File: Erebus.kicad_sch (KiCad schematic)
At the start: 28 parts, among them SW1 SW_SPST, U1 AMS1117-3.3, U2 H5VU25U, U3 H5VU25U, U4 AT32F415CBT7, U5 STM32F303CBTx, Y1 8MHz

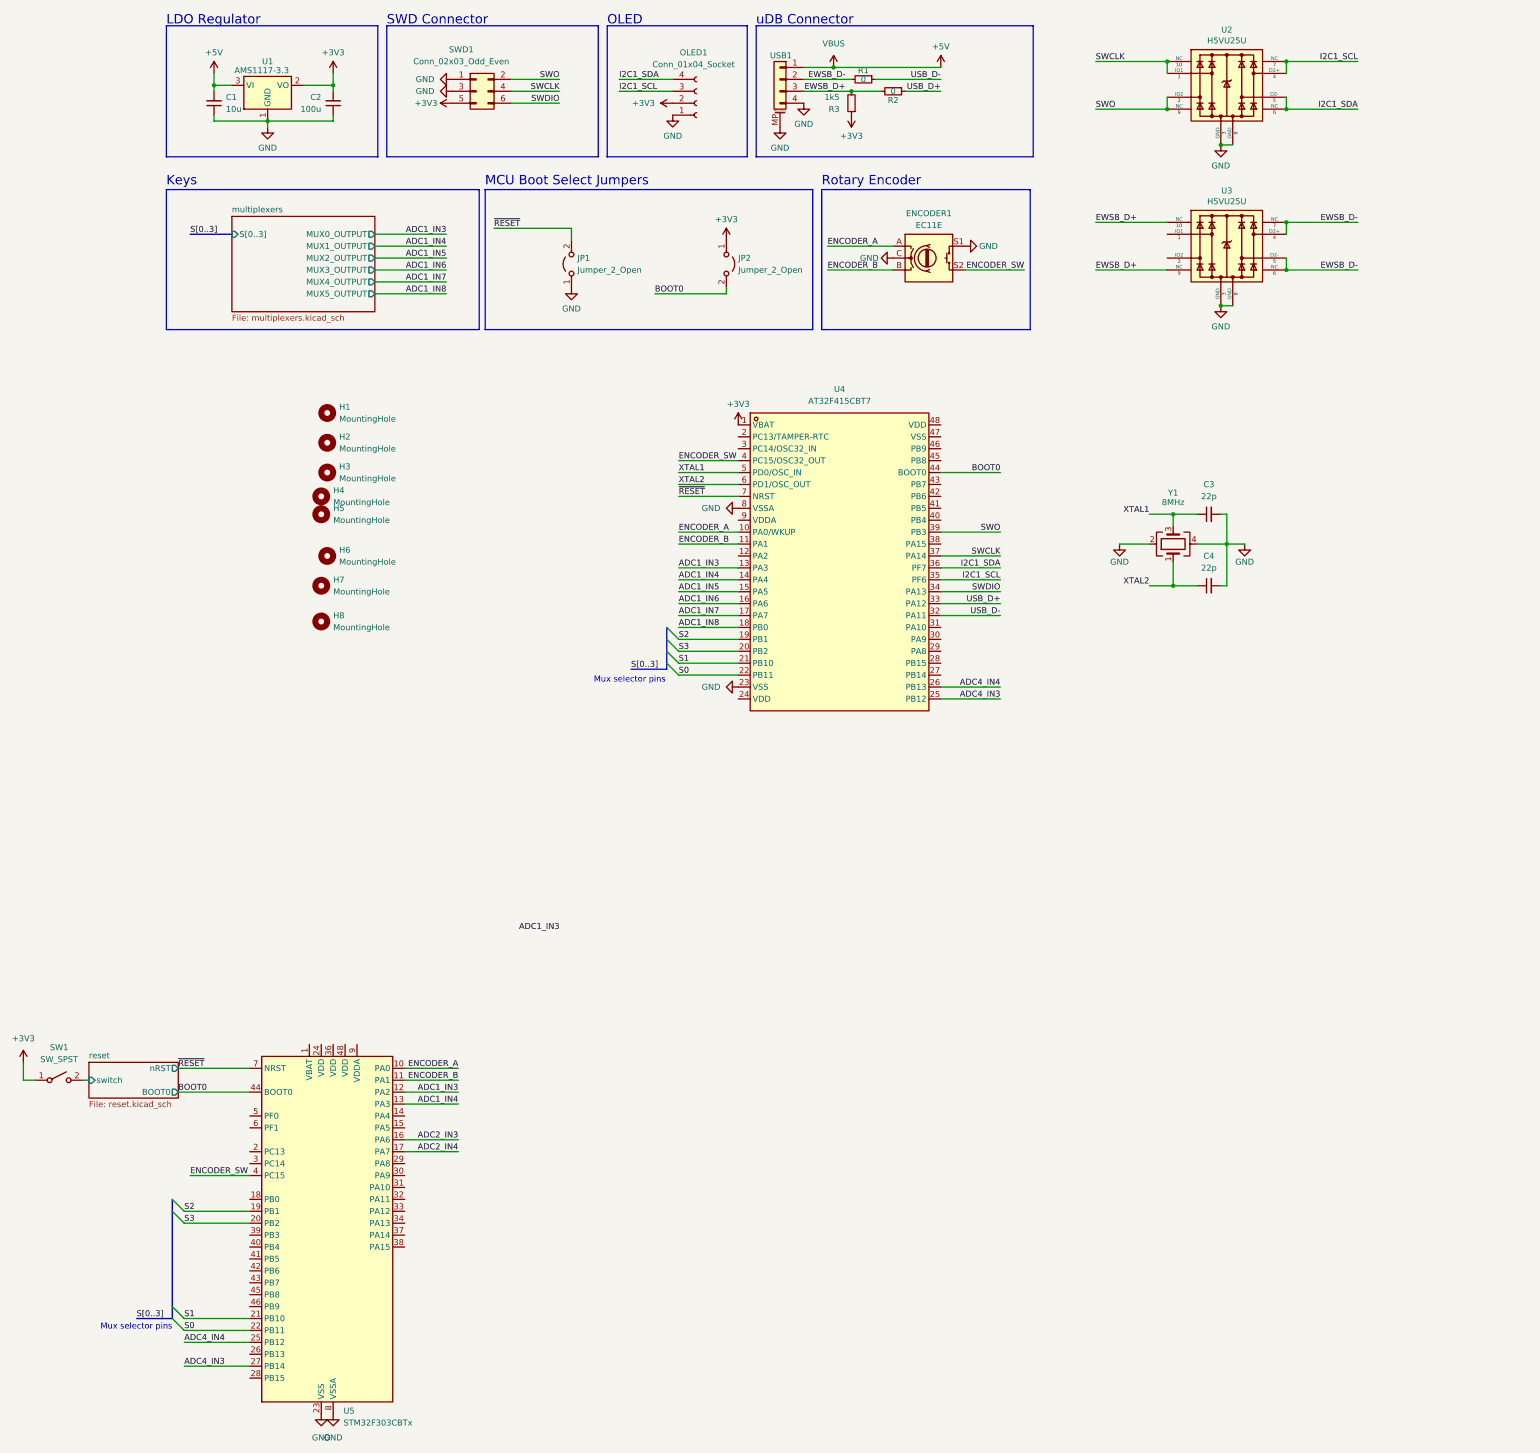
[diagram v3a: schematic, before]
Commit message: Switched to split layout ortholinear
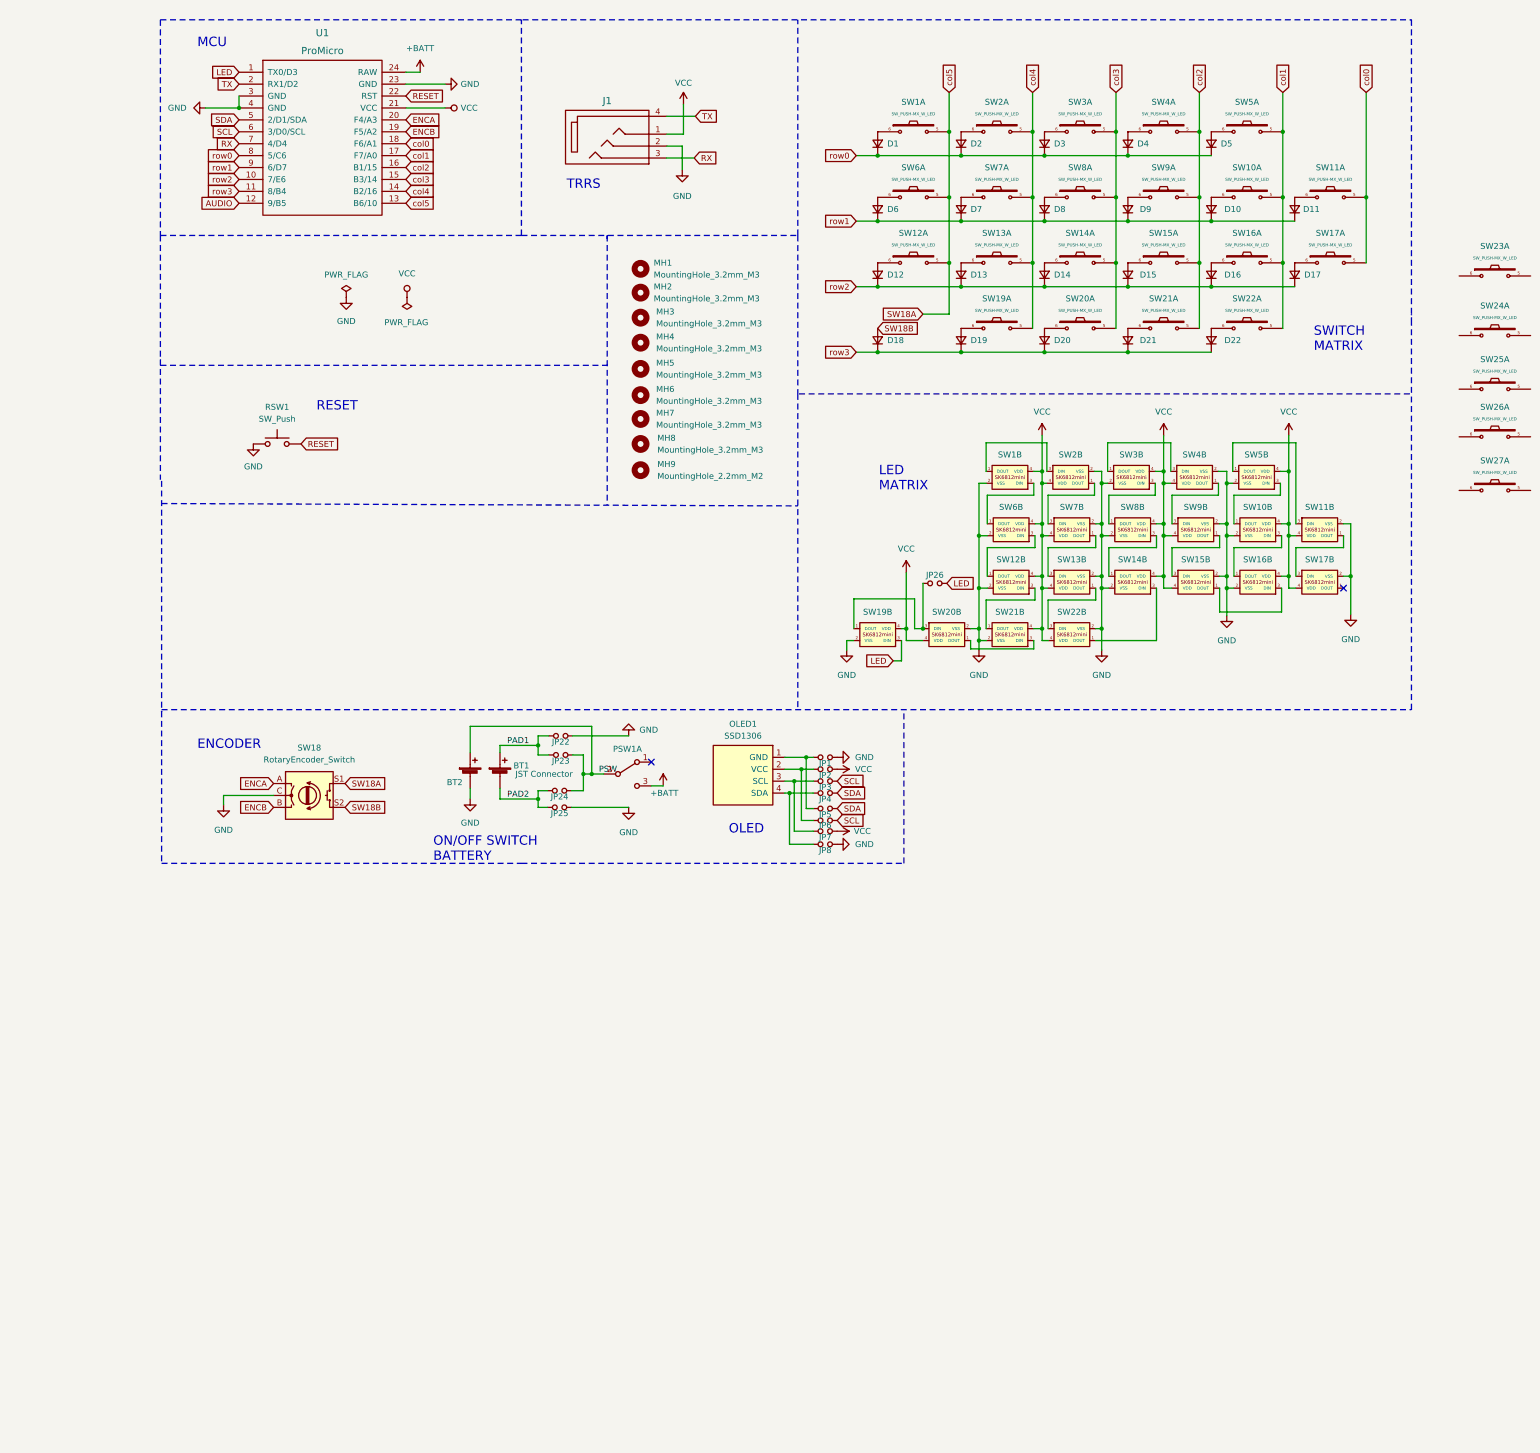
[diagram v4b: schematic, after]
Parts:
- removed C1: 10u, Capacitor_SMD:C_0402_1005Metric, symbol Device:C_Small
- removed C2: 100u, Capacitor_SMD:C_0402_1005Metric, symbol Device:C_Small
- removed C3, C4: 22p, Capacitor_SMD:C_0402_1005Metric, symbol Device:C_Small
- removed ENCODER1: EC11E, PCM_marbastlib-various:ROT_Alps_EC11E-Switch, symbol Device:RotaryEncoder_Switch
- removed H1, H2, H3, H4, H5, H6, H7, H8: MountingHole, MountingHole:MountingHole_2.2mm_M2_Pad, symbol Mechanical:MountingHole
- removed JP1, JP2: Jumper_2_Open, Connector_PinHeader_2.54mm:PinHeader_1x02_P2.54mm_Vertical, symbol Jumper:Jumper_2_Open
- removed OLED1: Conn_01x04_Socket, Erebus:OLED Module, symbol Connector:Conn_01x04_Socket
- removed R1, R2: 0, Resistor_SMD:R_0603_1608Metric_Pad0.98x0.95mm_HandSolder, symbol Device:R_Small
- removed R3: 1k5, Resistor_SMD:R_0402_1005Metric, symbol Device:R_Small
- removed SW1: SW_SPST, Button_Switch_SMD:SW_SPST_TL3342, symbol Switch:SW_SPST
- removed SWD1: Conn_02x03_Odd_Even, Connector_PinHeader_2.54mm:PinHeader_2x03_P2.54mm_Vertical, symbol Connector_Generic:Conn_02x03_Odd_Even
- removed U1: AMS1117-3.3, Package_TO_SOT_SMD:SOT-223-3_TabPin2, symbol Regulator_Linear:AMS1117-3.3
- removed U2, U3: H5VU25U, Erebus:DFN2510, symbol Unified-Daughterboard-rescue:TPD4E05U06DQAR-acheronSymbols
- removed U4: AT32F415CBT7, easyeda2kicad:LQFP-48_L7.0-W7.0-P0.50-LS9.0-BL, symbol easyeda2kicad:AT32F415CBT7
- removed U5: STM32F303CBTx, Package_QFP:LQFP-48_7x7mm_P0.5mm, symbol MCU_ST_STM32F3:STM32F303CBTx
- removed USB1: X1224WRS-04-LPV01, Erebus:PicoEZMate-Reinforced-Alt, symbol Connector_Generic_MountingPin:Conn_01x04_MountingPin
- removed Y1: 8MHz, Crystal:Crystal_SMD_3225-4Pin_3.2x2.5mm, symbol Device:Crystal_GND24
- added BT1: JST Connector, KLOR:JST_PH_reversible, symbol Device:Battery_Cell
- added BT2: Battery_Cell, KLOR:custombatteryconnector_small, symbol Device:Battery_Cell
- added D1, D10, D11, D12, D13, D14, D15, D16, D17, D18, D19, D2, D20, D21, D22, D3, D4, D5, D6, D7, D8, D9: D_Small, KLOR:Diode_SOD123, symbol Device:D_Small
- added J1: MJ-4PP-9, KLOR:MJ-4PP-9, symbol KLORlib:MJ-4PP-9 TRRS
- added JP1, JP2, JP22, JP23, JP24, JP25, JP26, JP3, JP4, JP5, JP6, JP7, JP8: Device_Jumper_NO_Small, KLOR:Jumper, symbol KLORlib:Device_Jumper_NO_Small
- added MH1, MH2, MH3, MH4, MH5, MH6, MH7, MH8: MountingHole_3.2mm_M3, MountingHole:MountingHole_3.2mm_M3, symbol Mechanical:MountingHole
- added MH9: MountingHole_2.2mm_M2, MountingHole:MountingHole_2.2mm_M2, symbol Mechanical:MountingHole
- added OLED1: SSD1306, KLOR:SSD1306_128x64OLED, symbol SSD1306-128x64_OLED:SSD1306
- added PSW1: SW_DPDT_x2, KLOR:MSK12C02_reversible, symbol Switch:SW_DPDT_x2
- added RSW1: SW_Push, KLOR:SW_Push_1P1T-MP_NO_Horizontal_Alps_SKRTLAE010_both_sides, symbol Switch:SW_Push
- added SW1, SW10, SW11, SW12, SW13, SW14, SW15, SW16, SW17, SW19, SW2, SW20, SW21, SW22, SW23, SW24, SW25, SW26, SW27, SW3, SW4, SW5, SW6, SW7, SW8, SW9: SW_PUSH-MX_W_LED, KLOR:SK6812MINI_and_cherry, symbol KLORlib:SW_PUSH-MX_W_LED
- added SW18: RotaryEncoder_Switch, KLOR:RotaryEncoder_Alps_EC11E-Switch_Vertical_H20mm-keebio_modified, symbol Device:RotaryEncoder_Switch
- added U1: ProMicro, KLOR:ProMicro, symbol Buzzard:ProMicro
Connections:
- net GND: now also BT2.2 (-), J1.2, JP1.2, JP22.2, JP25.2, JP8.2, RSW1.1, SW1.2 (VSS), SW10.2 (VSS), SW11.2 (VSS), SW12.2 (VSS), SW13.2 (VSS), SW14.2 (VSS), SW15.2 (VSS), SW16.2 (VSS), SW17.2 (VSS), SW18.C, SW19.2 (VSS), SW2.2 (VSS), SW20.2 (VSS), SW21.2 (VSS), SW22.2 (VSS), SW3.2 (VSS), SW4.2 (VSS), SW5.2 (VSS), SW6.2 (VSS), SW7.2 (VSS), SW8.2 (VSS), SW9.2 (VSS), U1.23 (GND), U1.3 (GND), U1.4 (GND)
- new net: SW1.3 (DIN), SW6.1 (DOUT)
- new net: SW12.1 (DOUT), SW6.3 (DIN)
- new net: SW12.3 (DIN), SW21.1 (DOUT)
- new net: SW20.1 (DOUT), SW21.3 (DIN)
- new net: D3.2 (A), SW3.6
- new net: D14.2 (A), SW14.6
- new net: D13.2 (A), SW13.6
- new net: D16.2 (A), SW16.6
- new net: D20.2 (A), SW20.6
- new net: SW15.3 (DIN), SW9.1 (DOUT)
- new net: SW4.1 (DOUT), SW9.3 (DIN)
- new net: D19.2 (A), SW19.6
- new net: SW3.3 (DIN), SW8.1 (DOUT)
- new net: SW14.1 (DOUT), SW8.3 (DIN)
- new net: JP1.1, JP5.1, OLED1.1 (GND)
- new net: JP2.1, JP6.1, OLED1.2 (VCC)
- new net: JP3.1, JP7.1, OLED1.3 (SCL)
- new net: JP4.1, JP8.1, OLED1.4 (SDA)
- new net: D9.2 (A), SW9.6
- new net: D15.2 (A), SW15.6
- new net: JP26.1, SW19.1 (DOUT), SW20.3 (DIN)
- new net: D4.2 (A), SW4.6
- new net: SW14.3 (DIN), SW22.1 (DOUT)
- new net: D7.2 (A), SW7.6
- new net: D6.2 (A), SW6.6
- new net: SW3.1 (DOUT), SW4.3 (DIN)
- new net: SW11.3 (DIN), SW5.1 (DOUT)
- new net: SW10.1 (DOUT), SW5.3 (DIN)
- new net: D1.2 (A), SW1.6
- new net: D5.2 (A), SW5.6
- new net: SW13.3 (DIN), SW7.1 (DOUT)
- new net: SW2.1 (DOUT), SW7.3 (DIN)
- new net: D21.2 (A), SW21.6
- new net: D2.2 (A), SW2.6
- new net: D17.2 (A), SW17.6
- new net: D12.2 (A), SW12.6
- new net: SW15.1 (DOUT), SW16.3 (DIN)
- new net: D10.2 (A), SW10.6
- new net: SW13.1 (DOUT), SW22.3 (DIN)
- new net: SW1.1 (DOUT), SW2.3 (DIN)
- new net: D11.2 (A), SW11.6
- new net: SW10.3 (DIN), SW16.1 (DOUT)
- new net: D8.2 (A), SW8.6
- new net: SW11.1 (DOUT), SW17.3 (DIN)
- new net: D22.2 (A), SW22.6
- new net +BATT: PSW1.3 (C), U1.24 (RAW)
- new net AUDIO: U1.12 (9/B5)
- new net ENCA: SW18.A, U1.20 (F4/A3)
- new net ENCB: SW18.B, U1.19 (F5/A2)
- new net LED: JP26.2, SW19.3 (DIN), U1.1 (TX0/D3)
- new net PAD1: BT1.1 (+), JP22.1, JP23.1
- new net PAD2: BT1.2 (-), JP24.1, JP25.1
- new net PSW: BT2.1 (+), JP23.2, JP24.2, PSW1.2 (B)
- new net RESET: RSW1.2, U1.22 (RST)
- new net RX: J1.3, U1.7 (4/D4)
- new net SCL: JP3.2, JP6.2, U1.6 (3/D0/SCL)
- new net SDA: JP4.2, JP5.2, U1.5 (2/D1/SDA)
- new net SW18A: SW1.5, SW12.5, SW18.S1, SW6.5, U1.13 (B6/10)
- new net SW18B: D18.2 (A), SW18.S2
- new net TX: J1.4, U1.2 (RX1/D2)
- new net VCC: J1.1, JP2.2, JP7.2, SW1.4 (VDD), SW10.4 (VDD), SW11.4 (VDD), SW12.4 (VDD), SW13.4 (VDD), SW14.4 (VDD), SW15.4 (VDD), SW16.4 (VDD), SW17.4 (VDD), SW19.4 (VDD), SW2.4 (VDD), SW20.4 (VDD), SW21.4 (VDD), SW22.4 (VDD), SW3.4 (VDD), SW4.4 (VDD), SW5.4 (VDD), SW6.4 (VDD), SW7.4 (VDD), SW8.4 (VDD), SW9.4 (VDD), U1.21 (VCC)
- new net col0: SW11.5, SW17.5, U1.18 (F6/A1)
- new net col1: SW10.5, SW16.5, SW22.5, SW5.5, U1.17 (F7/A0)
- new net col2: SW15.5, SW21.5, SW4.5, SW9.5, U1.16 (B1/15)
- new net col3: SW14.5, SW20.5, SW3.5, SW8.5, U1.15 (B3/14)
- new net col4: SW13.5, SW19.5, SW2.5, SW7.5, U1.14 (B2/16)
- new net row0: D1.1 (K), D2.1 (K), D3.1 (K), D4.1 (K), D5.1 (K), U1.8 (5/C6)
- new net row1: D10.1 (K), D11.1 (K), D6.1 (K), D7.1 (K), D8.1 (K), D9.1 (K), U1.9 (6/D7)
- new net row2: D12.1 (K), D13.1 (K), D14.1 (K), D15.1 (K), D16.1 (K), D17.1 (K), U1.10 (7/E6)
- new net row3: D18.1 (K), D19.1 (K), D20.1 (K), D21.1 (K), D22.1 (K), U1.11 (8/B4)
- no-connect marks 0 -> 2
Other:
- removed sheet multiplexers
- removed sheet reset
- note added: "ENCODER"
- note added: "LED MATRIX"
- note added: "MCU"
- note added: "ON/OFF SWITCH BATTERY"
- note added: "RESET"
- note added: "SWITCH MATRIX"
- note added: "TRRS"
- note removed: "Keys"
- note removed: "LDO Regulator"
- note removed: "MCU Boot Select Jumpers"
- note removed: "Mux selector pins"
- note removed: "Rotary Encoder"
- note removed: "SWD Connector"
- note removed: "uDB Connector"
- title: (none) -> Klor Split Keyboard

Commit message: Fixed title block
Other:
- title: Klor Split Keyboard -> Erebus Split Keyboard
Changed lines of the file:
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@@
 	(paper "A4")
 	(title_block
-		(title "Klor Split Keyboard")
-		(date "2022-06-21")
-		(rev "1.3")
-		(comment 1 "Schematic based on Sofle")
-		(comment 2 "Author: GEIST")
+		(title "Erebus Split Keyboard")
+		(date "2026-03-20")
+		(rev "1.0")
+		(comment 1 "Schematic based on Klor")
+		(comment 2 "Author: simaanc")
 	)
 	(text "SWITCH\nMATRIX"
